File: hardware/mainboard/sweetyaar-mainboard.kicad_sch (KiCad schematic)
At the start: 99 parts

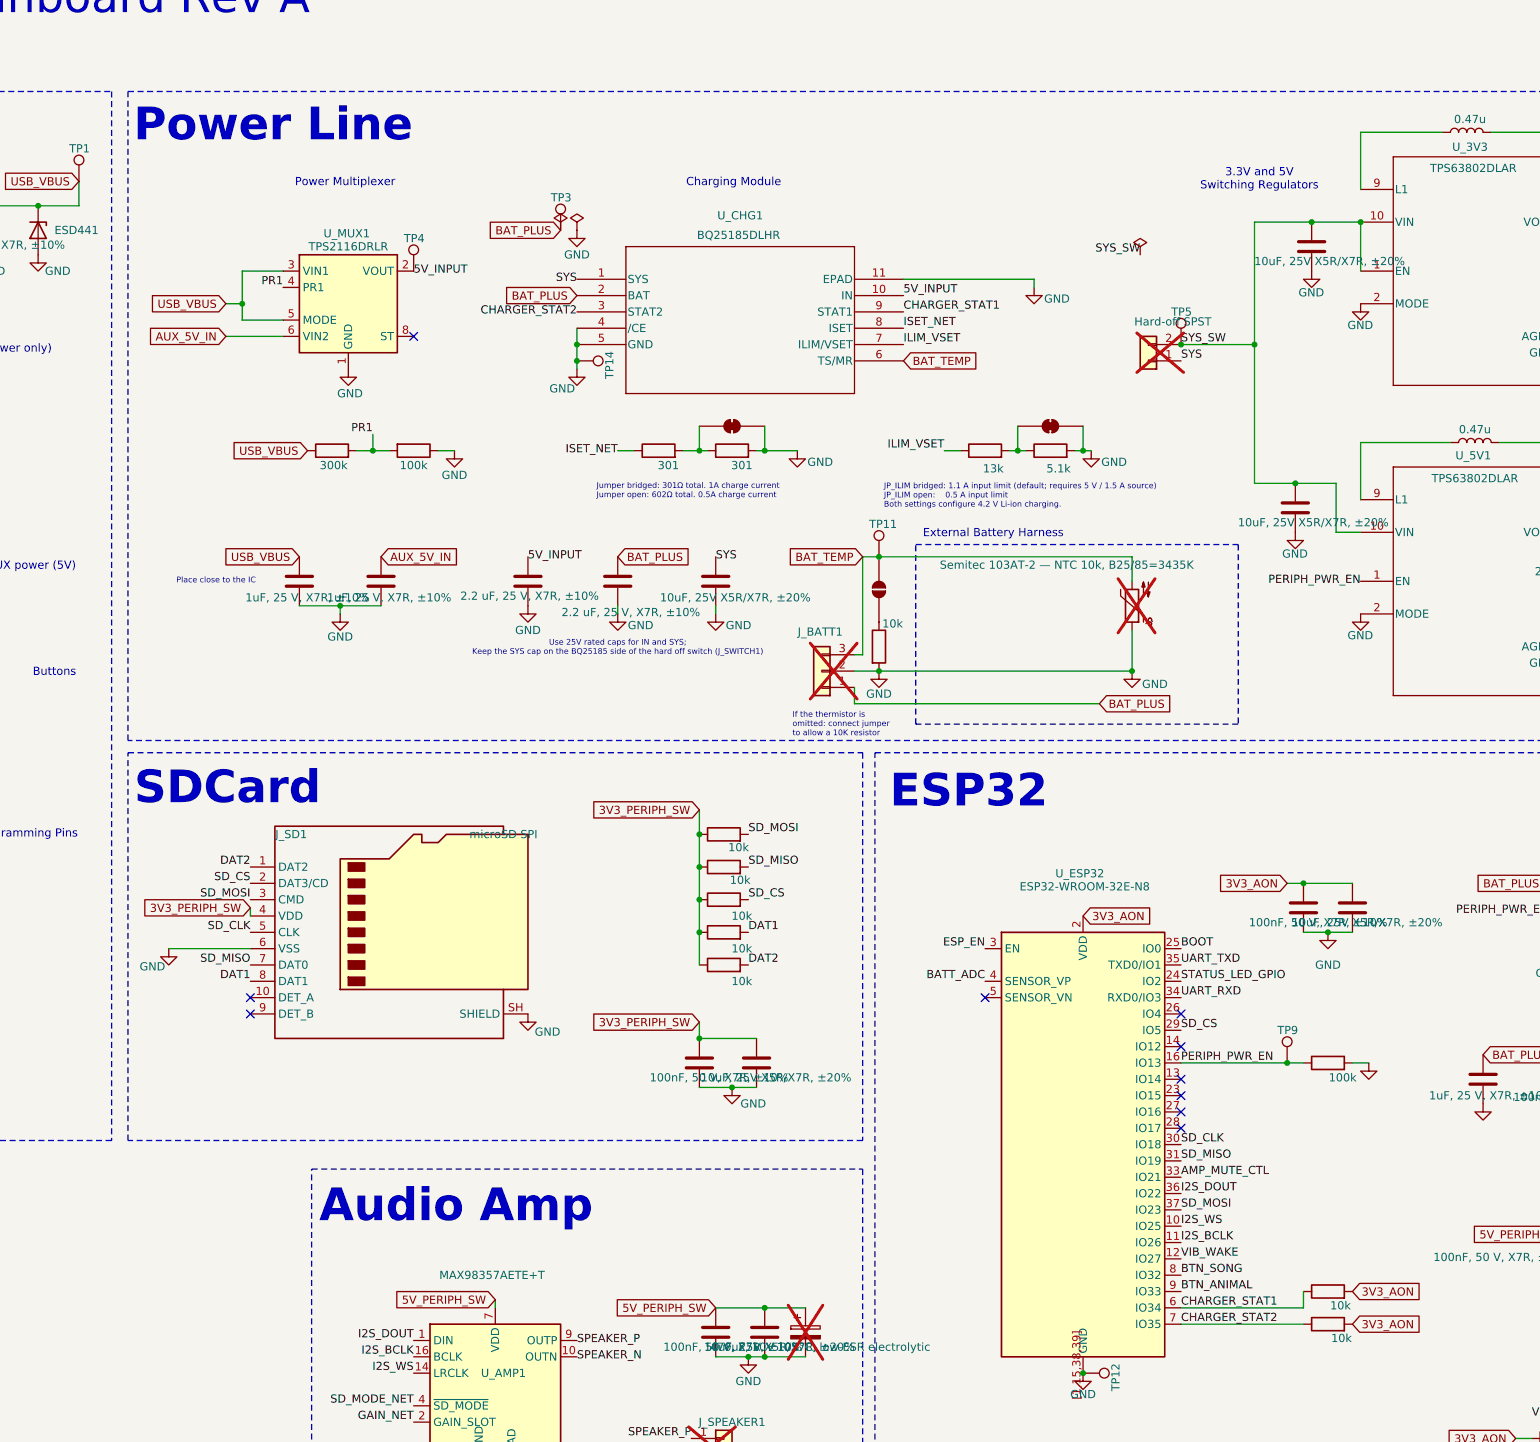
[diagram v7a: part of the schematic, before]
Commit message: Switch charger to firmware-supervised BQ25186
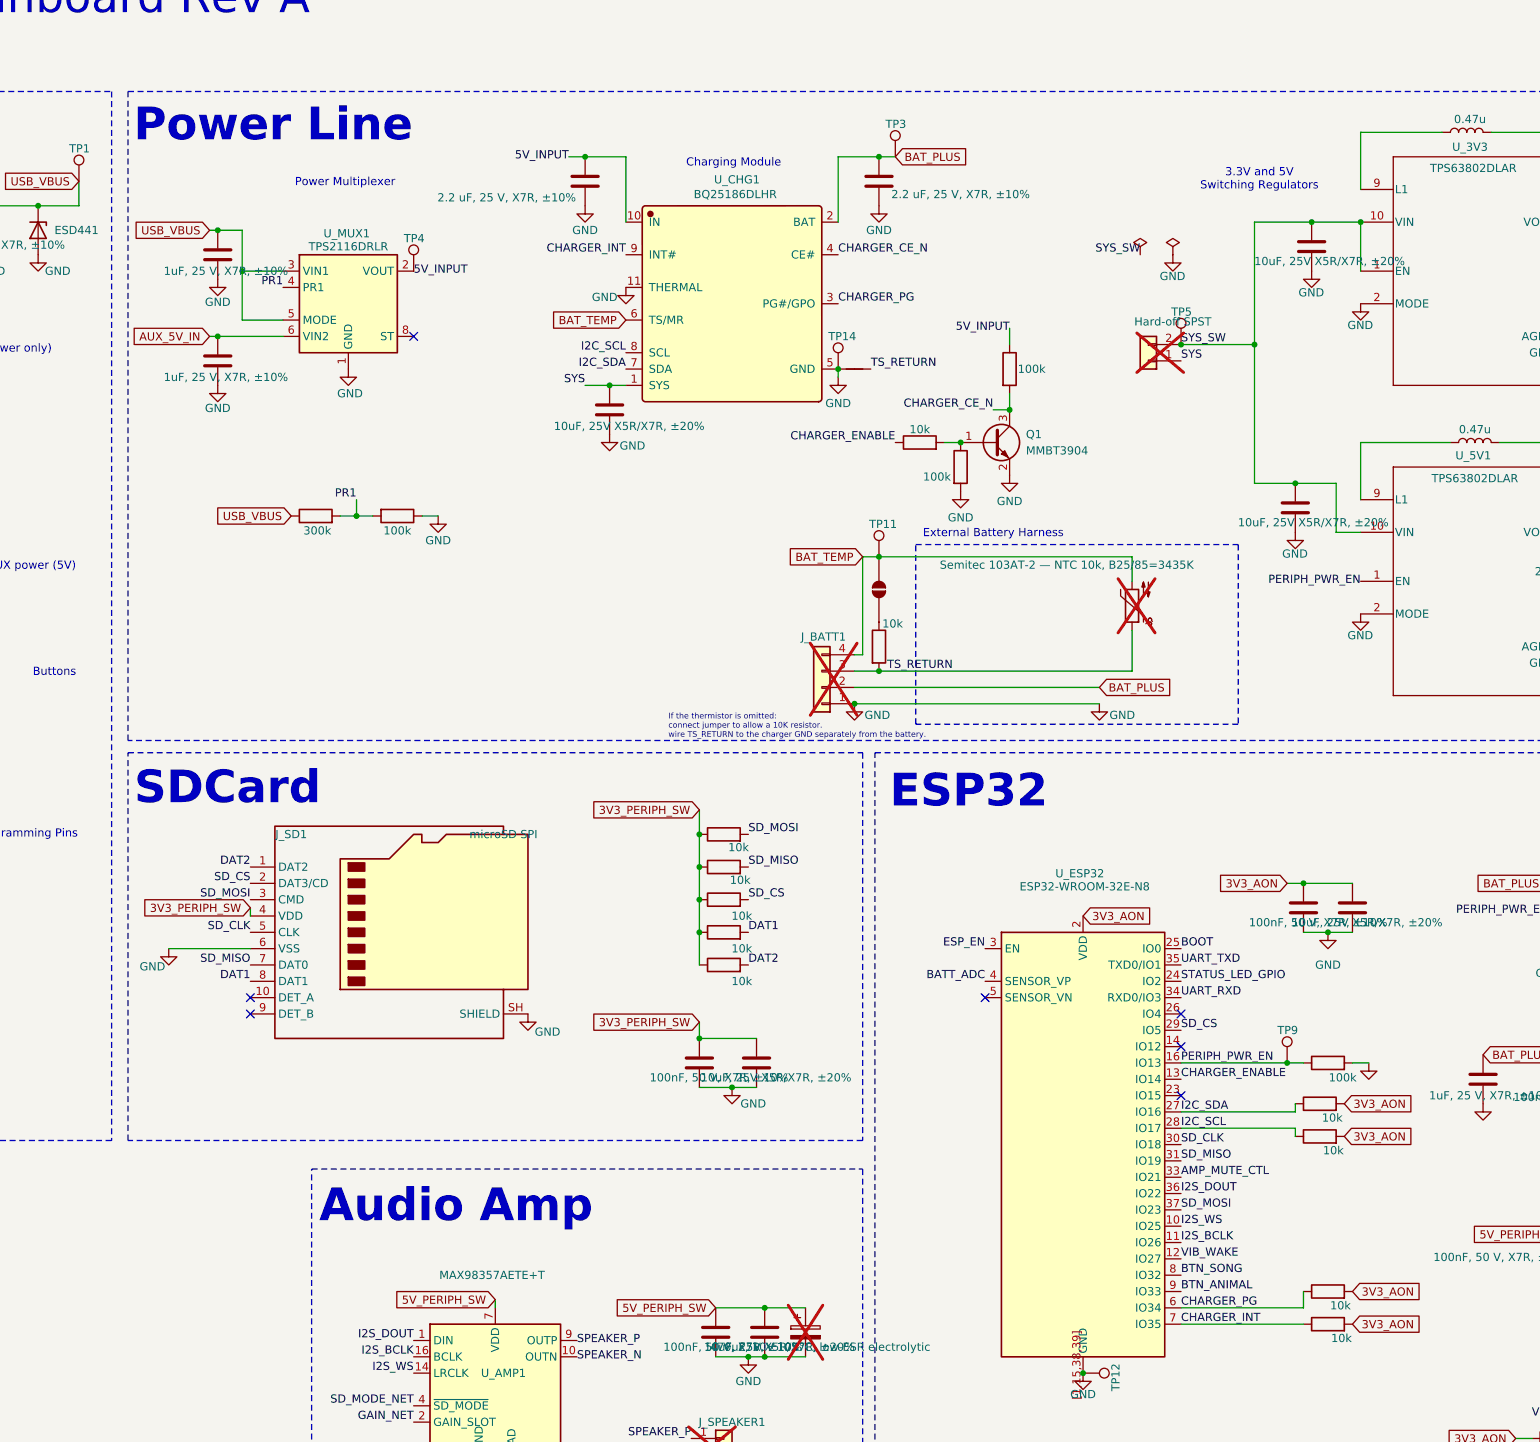
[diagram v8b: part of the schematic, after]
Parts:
- removed JP_ILIM1: JP_ILIM, Jumper:SolderJumper-2_P1.3mm_Bridged_RoundedPad1.0x1.5mm, symbol Jumper:SolderJumper_2_Bridged
- removed JP_ISET1: JP_ISET, Jumper:SolderJumper-2_P1.3mm_Bridged_RoundedPad1.0x1.5mm, symbol Jumper:SolderJumper_2_Bridged
- removed R_ILIM1: 5.1k, Resistor_SMD:R_0603_1608Metric, symbol Device:R
- removed R_ILIM2: 13k, Resistor_SMD:R_0603_1608Metric, symbol Device:R
- removed R_ISET1, R_ISET2: 301, Resistor_SMD:R_0603_1608Metric, symbol Device:R
- added NT1: NetTie_2, NetTie:NetTie-2_SMD_Pad0.5mm, symbol Device:NetTie_2
- added Q1: MMBT3904, Package_TO_SOT_SMD:SOT-23, symbol Transistor_BJT:MMBT3904
- added R_CHARGER_CE_BASE1, R_SCL1, R_SDA1: 10k, Resistor_SMD:R_0603_1608Metric, symbol Device:R
- added R_CHARGER_CE_PD1, R_CHARGER_CE_PU1: 100k, Resistor_SMD:R_0603_1608Metric, symbol Device:R
- J_BATT1: footprint Connector_JST:JST_XH_B3B-XH-A_1x03_P2.50mm_Vertical -> Connector_JST:JST_XH_B4B-XH-A_1x04_P2.50mm_Vertical; symbol Connector_Generic:Conn_01x03 -> Connector_Generic:Conn_01x04; LCSC C144394 -> C144395
- U_CHG1: value BQ25185DLHR -> BQ25186DLHR; symbol SweetYaar:BQ25185DLHR -> LCSC:BQ25186DLHR_C44639442; LCSC C19725033 -> C44639442; Manufacturer (none) -> Texas Instruments; Manufacturer Part (none) -> BQ25186DLHR
- renumbered R_STAT2 to R_INT1, R_STAT1 to R_PG1
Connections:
- net ILIM_VSET is gone; now on net I2C_SDA: U_CHG1.7 (SDA)
- net ISET_NET is gone; now on net I2C_SCL: U_CHG1.8 (SCL)
- net 3V3_AON: now also R_SCL1.2, R_SDA1.2
- net 5V_INPUT: now also R_CHARGER_CE_PU1.1
- net BAT_PLUS: now also J_BATT1.2 (Pin_2); no longer J_BATT1.1 (Pin_1)
- net BAT_TEMP: now also J_BATT1.4 (Pin_4); no longer J_BATT1.3 (Pin_3)
- net GND: now also J_BATT1.1 (Pin_1), NT1.1, Q1.2 (E), R_CHARGER_CE_PD1.2; no longer J_BATT1.2 (Pin_2), R_TH1.2, TH1.1, U_CHG1.4 (/CE)
- net CHARGER_ENABLE: now reaches U_ESP32.13 (IO14)
- net CHARGER_ENABLE: now also R_CHARGER_CE_BASE1.1
- net I2C_SDA: now reaches U_ESP32.27 (IO16)
- net I2C_SDA: now also R_SDA1.1
- net I2C_SCL: now reaches U_ESP32.28 (IO17)
- net I2C_SCL: now also R_SCL1.1
- net CHARGER_STAT1 renamed CHARGER_PG
- net CHARGER_PG: now also U_CHG1.3 (PG#/GPO); no longer U_CHG1.9 (STAT1)
- net CHARGER_STAT2 renamed CHARGER_INT
- net CHARGER_INT: now also U_CHG1.9 (INT#); no longer U_CHG1.3 (STAT2)
- new net: Q1.1 (B), R_CHARGER_CE_BASE1.2, R_CHARGER_CE_PD1.1
- new net CHARGER_CE_N: Q1.3 (C), R_CHARGER_CE_PU1.2, U_CHG1.4 (CE#)
- new net TS_RETURN: J_BATT1.3 (Pin_3), NT1.2, R_TH1.2, TH1.1
- no-connect marks 18 -> 15
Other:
- note added: "If the thermistor is omitted: connect jumper to allow a 10K resistor. wire TS_RETURN to the charger GND separately from the battery."
- note removed: "If the thermistor is omitted: connect jumper to allow a 10K resistor"
- note removed: "JP_ILIM bridged: 1.1 A input limit (default; requires 5 V / 1.5 A source) JP_ILIM open: 0.5 A input limit Both settings configure 4.2 V Li-ion charging."
- note removed: "Jumper bridged: 301Ω total. 1A charge current Jumper open: 602Ω total. 0.5A charge current"
- note removed: "Place close to the IC"
- note removed: "Use 25V rated caps for IN and SYS; Keep the SYS cap on the BQ25185 side of the hard off switch (J_SWITCH1)"
- moved on the sheet: TP14, TP3, U_CHG1
